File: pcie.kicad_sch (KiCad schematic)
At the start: 23 parts, among them J10 Socket_Amphenol_ME10168134011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, J11 PCB-Edge_M.2_Key-M, J12 OCuLink_x4_Amphenol_G14A42121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

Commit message: [#92504] Wire OCuLink
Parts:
- removed C27, C28, C29, C30: C_100n_16V_X7R_0402, antmicro-footprints:C_0402_1005Metric, symbol Capacitors0402:C_100n_16V_X7R_0402
- removed J10: Socket_Amphenol_ME1016813401101, antmicro-footprints:Socket_DC-SCM-2.1_2x84_Rev-1-1, symbol antmicroEdgeConnectors:Socket_DC-SCM-2.1_2x84_Rev-1-1
- removed J11: PCB-Edge_M.2_Key-M, antmicro-footprints:PCB-Edge_M.2_Key-M, symbol EdgeConnectors:PCB-Edge_M.2_Key-M
- removed J12: OCuLink_x4_Amphenol_G14A421211112HR, antmicro-footprints:Amphenol_G14A421211112HR, symbol PciConnectors:OCuLink_x4_Amphenol_G14A421211112HR
- removed R42, R43, R53: R_0R_0402, antmicro-footprints:R_0402_1005Metric, symbol Resistors0402:R_0R_0402
- removed R44, R45, R46, R47, R48, R49, R50, R51: R_0R_0201, antmicro-footprints:R_0201, symbol antmicroResistorsmisc:R_0R_0201
- removed R52: R_0R_0402, antmicro-footprints:R_0402_1005Metric, symbol antmicroResistors0402:R_0R_0402
- removed TP4, TP5: TP_1.5mm_SMD, antmicro-footprints:TP_SMD_1.5mm, symbol TestPoints:TP_1.5mm_SMD
- removed TP6: TP_1mm_SMD, antmicro-footprints:TP_SMD_1mm, symbol antmicroTestPoints:TP_1mm_SMD
- added C27, C28: C_100n_16V_X7R_0402, antmicro-footprints:C_0402_1005Metric, symbol antmicroCapacitors0402:C_100n_16V_X7R_0402
- added J11: OCuLink_x4_Amphenol_G14A421211112HR, antmicro-footprints:Amphenol_G14A421211112HR, symbol antmicroPciConnectors:OCuLink_x4_Amphenol_G14A421211112HR
- added R42, R43, R44, R45, R46, R47, R48, R49: R_0R_0402, antmicro-footprints:R_0402_1005Metric, symbol antmicroResistors0402:R_0R_0402
- added TP58: TP_0.75mm_SMD, antmicro-footprints:TP_SMD_0.75mm, symbol antmicroTestPoints:TP_0.75mm_SMD
- R41: now not fitted
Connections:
- net DC-SCM_CLK_100M_0.CLK+: now also R41.1, R43.2
- net DC-SCM_CLK_100M_0.CLK-: now also R42.1, R45.2
- net DC-SCM_PCIE1.RX0+: now also J11.A3 (PER0+)
- net DC-SCM_PCIE1.RX0-: now also J11.A4 (PER0-)
- net DC-SCM_PCIE1.TX0+: now also J11.B3 (PET0+)
- net DC-SCM_PCIE1.TX0-: now also J11.B4 (PET0-)
- net DC-SCM_PCIE_USB_SCMROOT.RX0+: now also J11.B6 (PET1+)
- net DC-SCM_PCIE_USB_SCMROOT.RX0-: now also J11.B7 (PET1-)
- net DC-SCM_PCIE_USB_SCMROOT.TX0+: now also J11.A6 (PER1+)
- net DC-SCM_PCIE_USB_SCMROOT.TX0-: now also J11.A7 (PER1-)
- net GND: now also C27.1, C28.1, J11.A11 (GND), J11.A14 (GND), J11.A17 (GND), J11.A2 (GND), J11.A20 (GND), J11.A5 (GND), J11.A8 (GND), J11.B11 (GND), J11.B14 (GND), J11.B17 (GND), J11.B2 (GND), J11.B20 (GND), J11.B5 (GND), J11.B8 (GND), J11.SH; no longer R41.2
- net PCIe_{REF0}_R.CK+: now also J11.A12 (VSP1), R43.1, R44.1
- net PCIe_{REF0}_R.CK-: now also J11.A13 (VSP2), R45.1
- net ~{CPRSNT}: now also J11.B13 (~{CPRSNT}), R42.2, R48.1
- net ~{PERSTC}: now also R41.2, J11.B12 (~{PERST}), R47.1
- net ~{PERST}: now also R44.2, R47.2
- net ~{WAKEC}: now also J11.A10 (~{CWAKE}), R46.1, R49.1
- net ~{WAKE_C}_alt: now also R46.2
- net ~{WAKE}: now also R49.2
- new net: R48.2, TP58.1
- new net: C28.2, J11.B21 (V_{ACT}_TX_3V3)
- new net: C27.2, J11.A1 (V_{ACT}_RX_3V3)
- new net: J11.A21 (5V), J11.B1 (5V)
- no-connect marks 13 -> 11
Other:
- note added: "OCuLink"
- note removed: "PCIe directions from HPM POV"
- note removed: "Used as test pads"

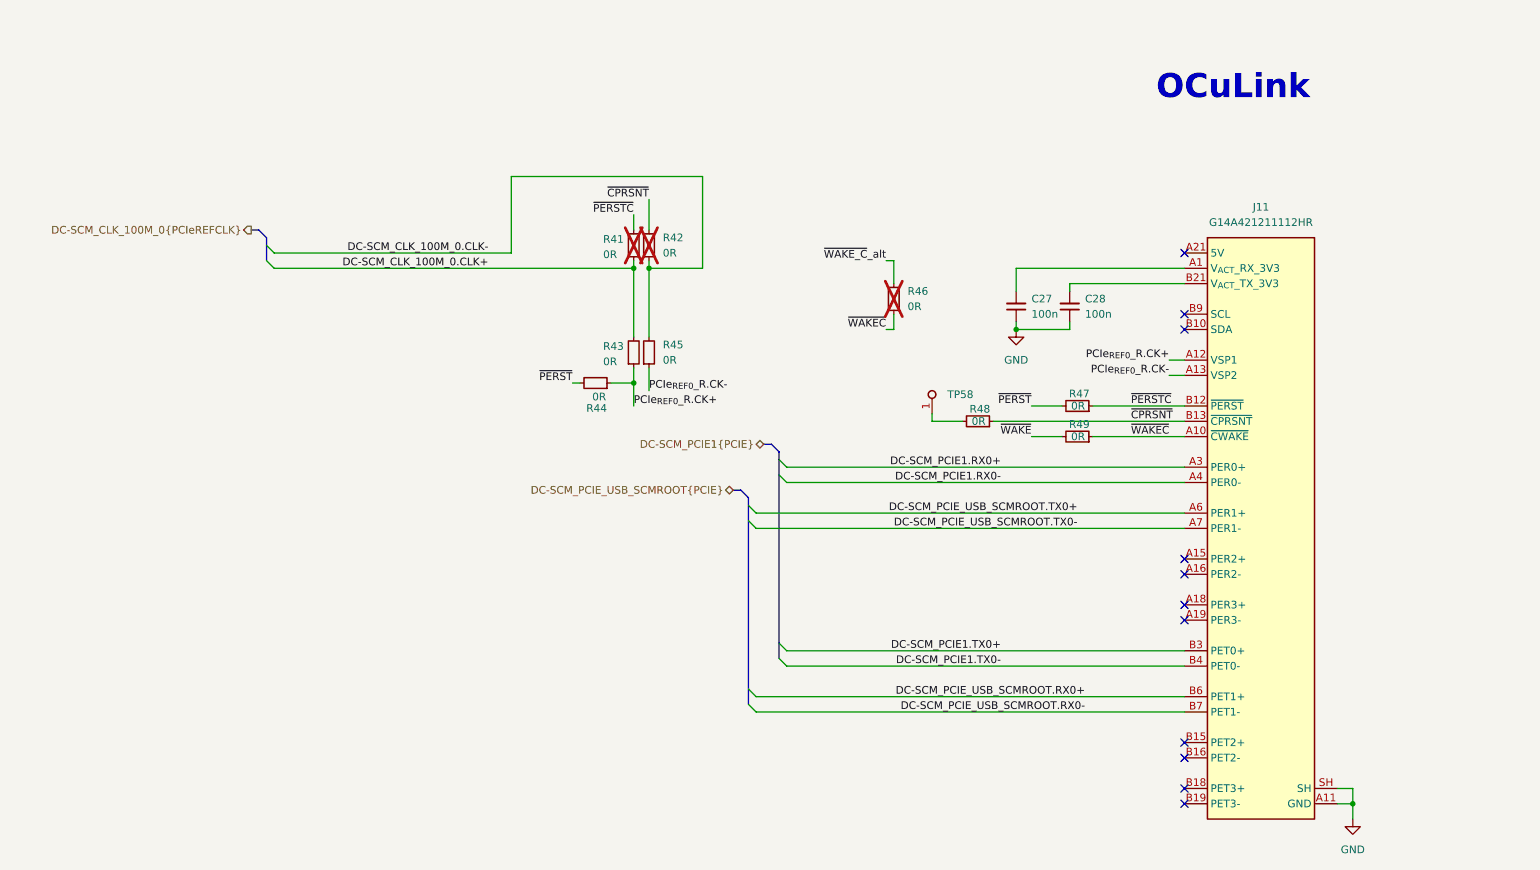
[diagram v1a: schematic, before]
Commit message: [#92504] Add power to OCuLink, add NC and 0R resistors
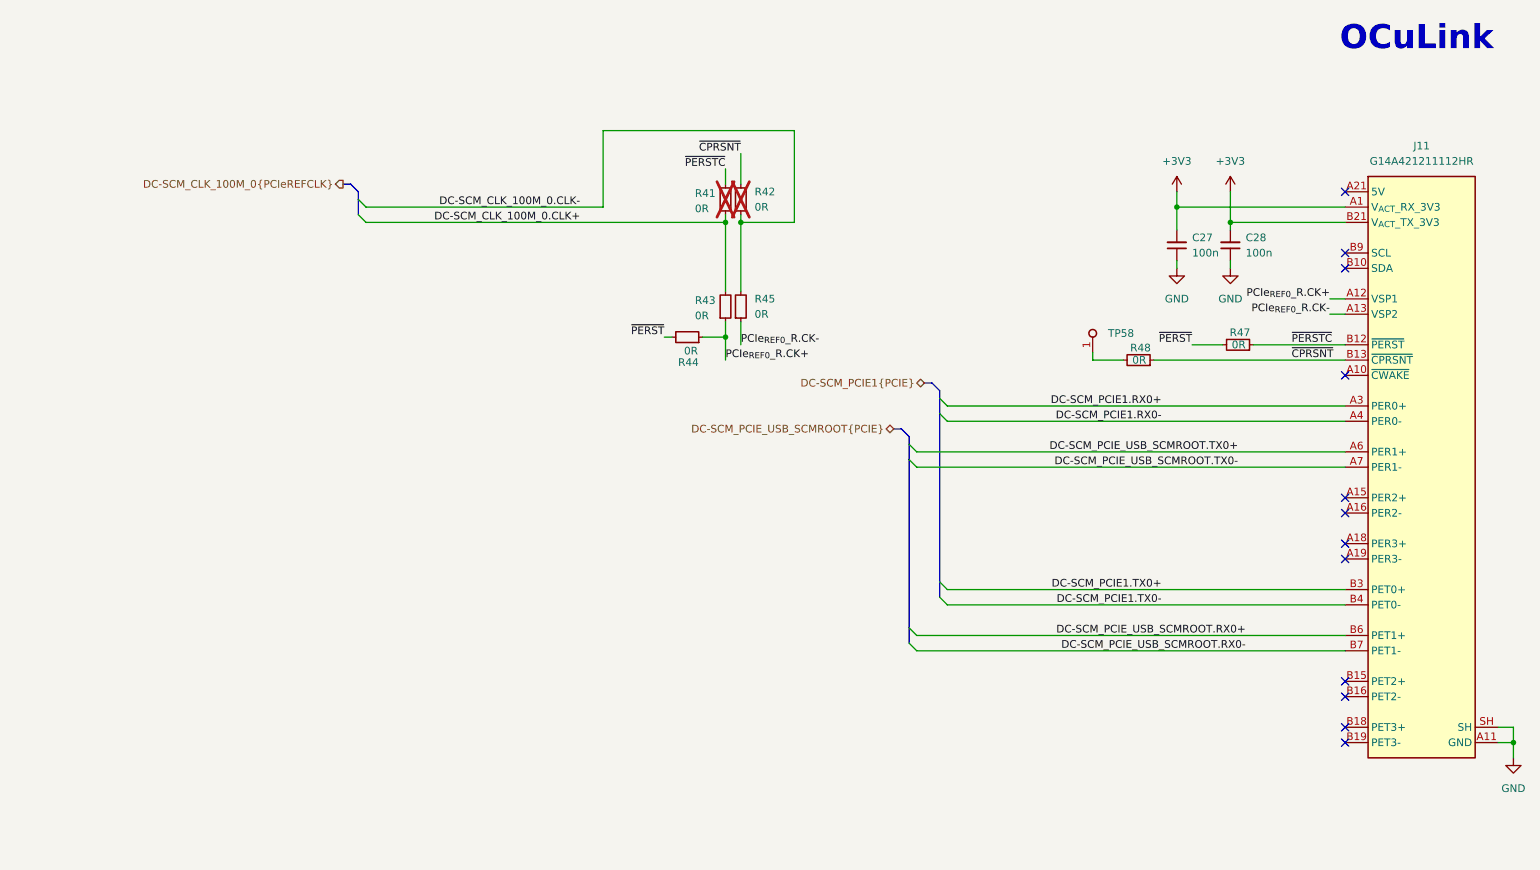
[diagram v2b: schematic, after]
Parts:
- removed R46, R49: R_0R_0402, antmicro-footprints:R_0402_1005Metric, symbol antmicroResistors0402:R_0R_0402
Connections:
- net +3V3: now reaches C28.2, J11.B21 (V_{ACT}_TX_3V3)
- net +3V3: now also C27.2, J11.A1 (V_{ACT}_RX_3V3)
- net ~{WAKEC}: no longer names the net of J11.A10 (~{CWAKE})
- no-connect marks 11 -> 12
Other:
- moved on the sheet: C27, C28, J11, R41, R42, R43, R44, R45, R47, R48, TP58

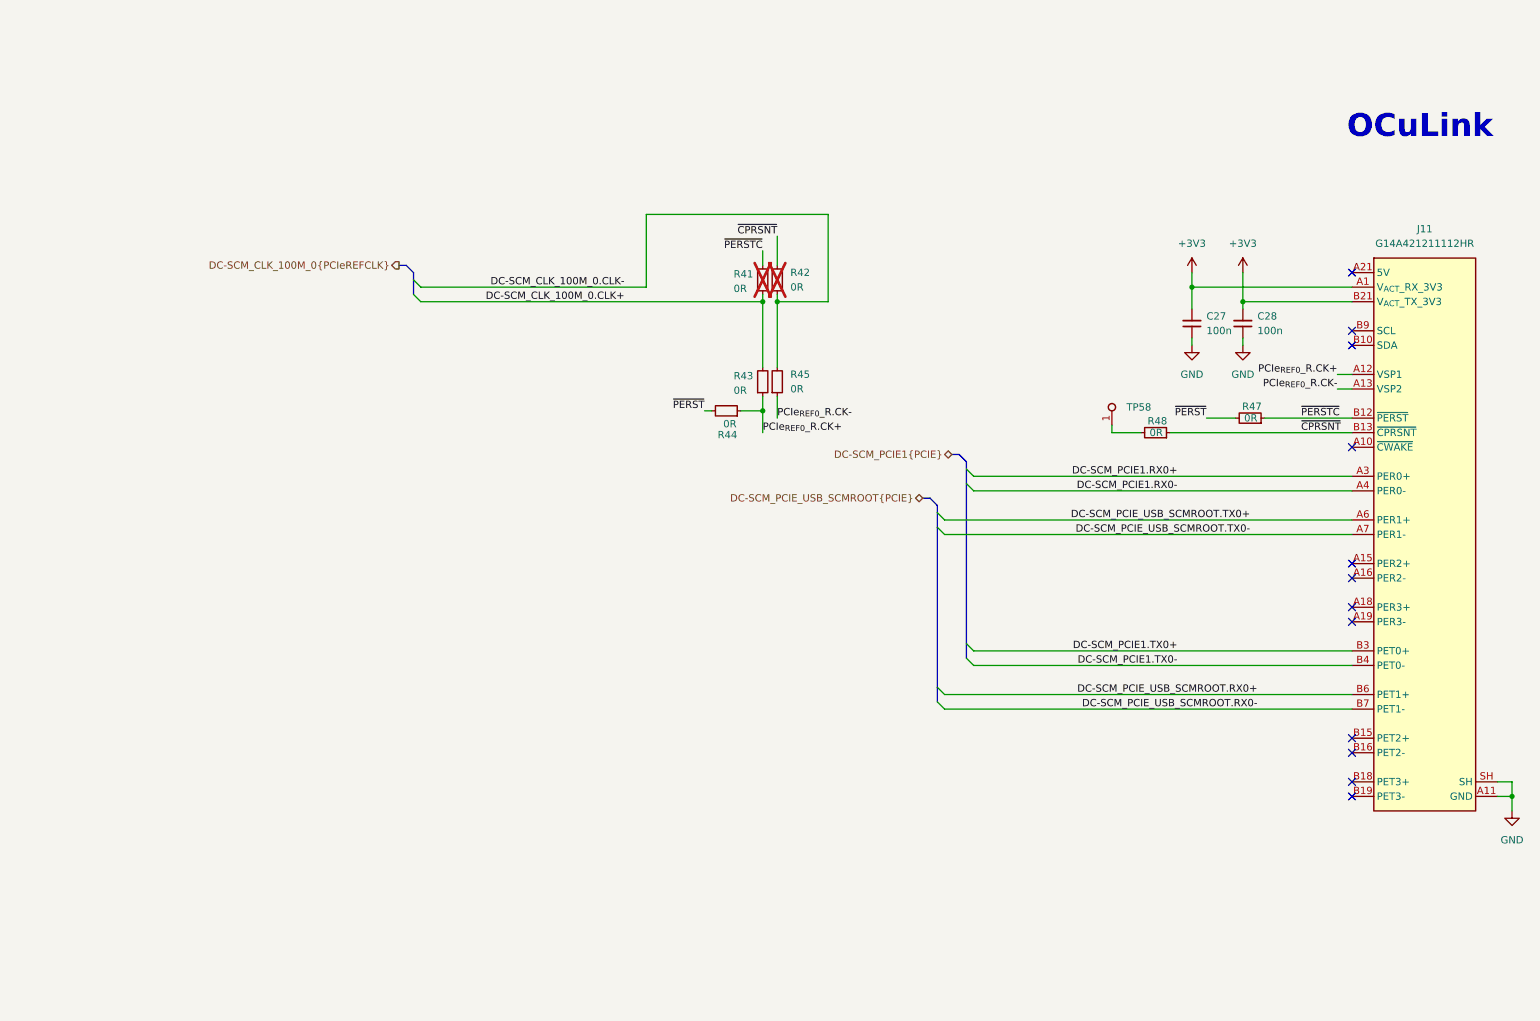
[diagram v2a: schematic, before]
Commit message: [#92504] Add second OCuLink
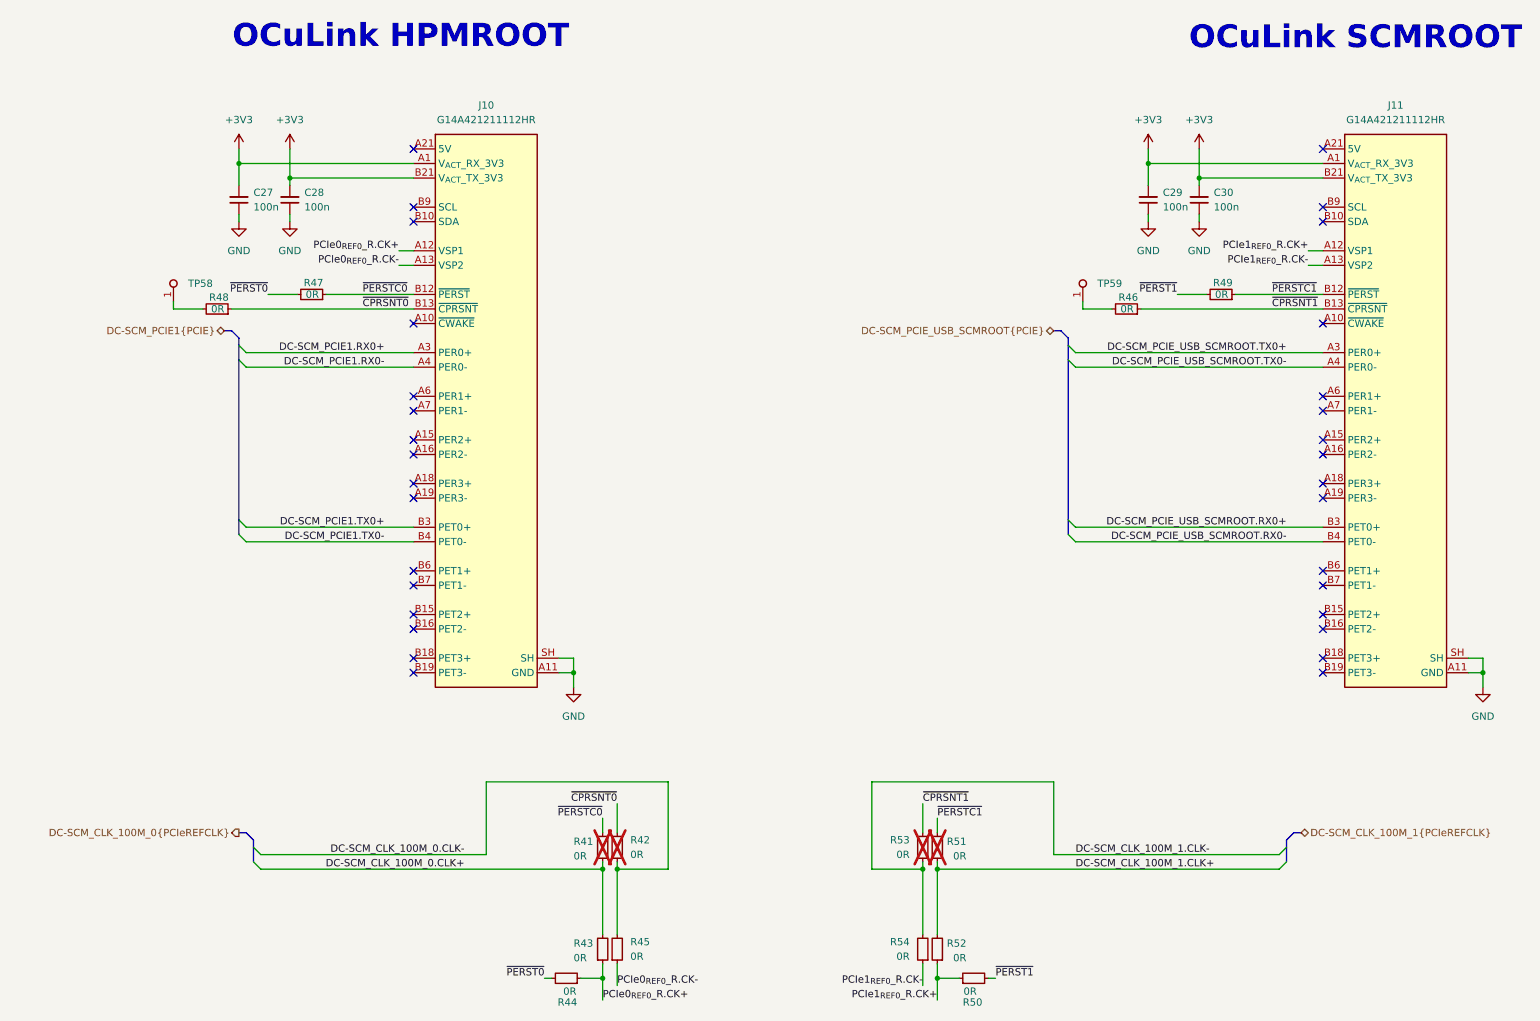
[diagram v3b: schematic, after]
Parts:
- added C29, C30: C_100n_16V_X7R_0402, antmicro-footprints:C_0402_1005Metric, symbol antmicroCapacitors0402:C_100n_16V_X7R_0402
- added J11: OCuLink_x4_Amphenol_G14A421211112HR, antmicro-footprints:Amphenol_G14A421211112HR, symbol antmicroPciConnectors:OCuLink_x4_Amphenol_G14A421211112HR
- added R46, R49, R50, R51, R52, R53, R54: R_0R_0402, antmicro-footprints:R_0402_1005Metric, symbol antmicroResistors0402:R_0R_0402
- added TP59: TP_0.75mm_SMD, antmicro-footprints:TP_SMD_0.75mm, symbol antmicroTestPoints:TP_0.75mm_SMD
- renumbered J11 to J10
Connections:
- net +3V3: now also C29.2, C30.2, J11.A1 (V_{ACT}_RX_3V3), J11.B21 (V_{ACT}_TX_3V3)
- net DC-SCM_PCIE_USB_SCMROOT.RX0+: now also J11.B3 (PET0+); no longer J10.B6 (PET1+)
- net DC-SCM_PCIE_USB_SCMROOT.RX0-: now also J11.B4 (PET0-); no longer J10.B7 (PET1-)
- net DC-SCM_PCIE_USB_SCMROOT.TX0+: now also J11.A3 (PER0+); no longer J10.A6 (PER1+)
- net DC-SCM_PCIE_USB_SCMROOT.TX0-: now also J11.A4 (PER0-); no longer J10.A7 (PER1-)
- net GND: now also C29.1, C30.1, J11.A11 (GND), J11.A14 (GND), J11.A17 (GND), J11.A2 (GND), J11.A20 (GND), J11.A5 (GND), J11.A8 (GND), J11.B11 (GND), J11.B14 (GND), J11.B17 (GND), J11.B2 (GND), J11.B20 (GND), J11.B5 (GND), J11.B8 (GND), J11.SH
- net PCIe_{REF0}_R.CK+ renamed PCIe0_{REF0}_R.CK+
- net PCIe_{REF0}_R.CK- renamed PCIe0_{REF0}_R.CK-
- net ~{CPRSNT} renamed ~{CPRSNT0}
- net ~{PERSTC} renamed ~{PERSTC0}
- net ~{PERST} renamed ~{PERST0}
- new net: R46.2, TP59.1
- new net: J11.A21 (5V), J11.B1 (5V)
- new net DC-SCM_CLK_100M_1.CLK+: R51.1, R52.2
- new net DC-SCM_CLK_100M_1.CLK-: R53.1, R54.2
- new net PCIe1_{REF0}_R.CK+: J11.A12 (VSP1), R50.1, R52.1
- new net PCIe1_{REF0}_R.CK-: J11.A13 (VSP2), R54.1
- new net ~{CPRSNT1}: J11.B13 (~{CPRSNT}), R46.1, R53.2
- new net ~{PERST1}: R49.2, R50.2
- new net ~{PERSTC1}: J11.B12 (~{PERST}), R49.1, R51.2
- no-connect marks 12 -> 32
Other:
- note added: "OCuLink HPMROOT"
- note added: "OCuLink SCMROOT"
- note removed: "OCuLink"
- moved on the sheet: C27, C28, J10, R41, R42, R43, R44, R45, R47, R48, TP58
